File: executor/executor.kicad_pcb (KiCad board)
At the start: 4 copper layers, 58 x 58 mm, 130 parts, among them J1 XT30PW(2+2), J2 gh1.25, 3p, J3 Conn_01x04, Q1 WNM6006, Q2 WNM6006, Q3 WNM6006, Q4 WNM6006, Q5 WNM6006, Q6 WNM6006, U1 TPS5430DDAR, U2 DRV8323SRTAT, U3 GD32F303RETx, U4 TCAN4550RGYRQ1, U5 AS5047P-ATSM, U6 QMA7981, Y1 8M, Y2 40M

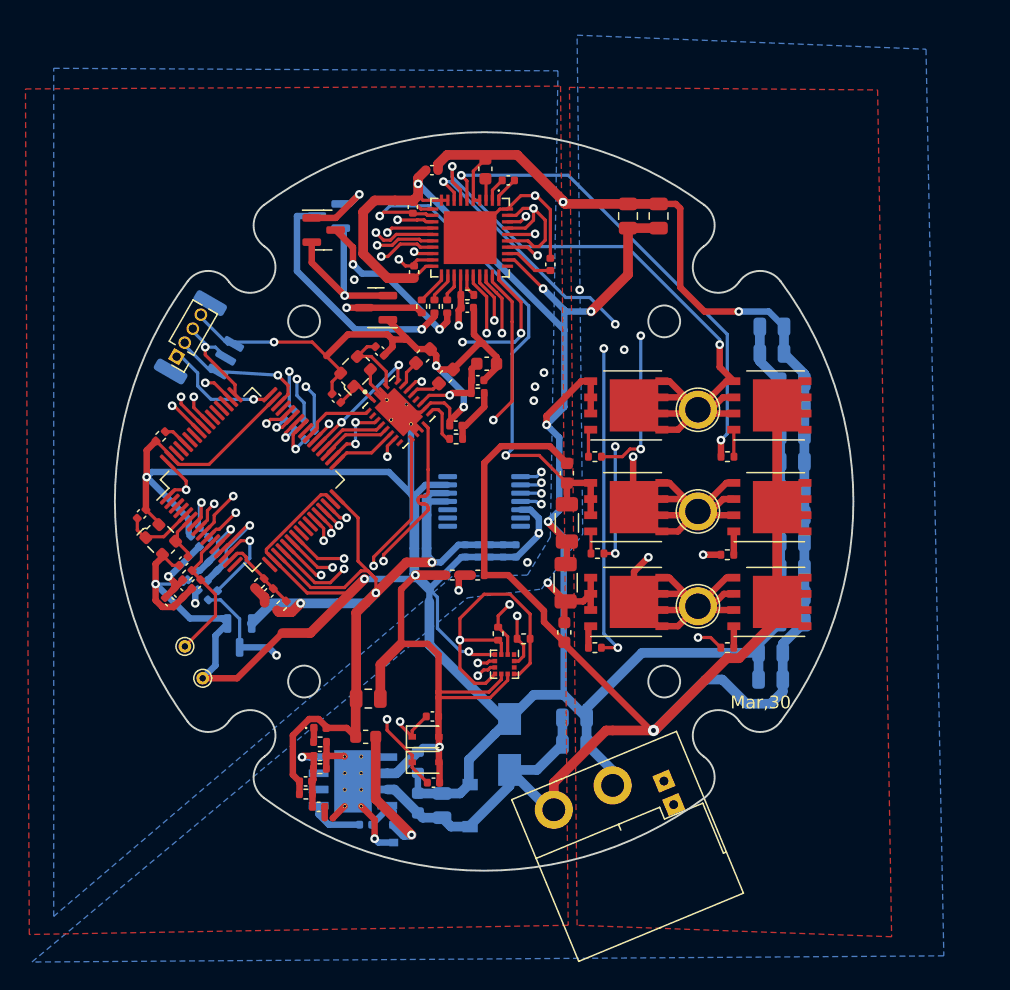
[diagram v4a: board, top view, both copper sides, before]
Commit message: [New] Complete PCB layout of executor v2.0
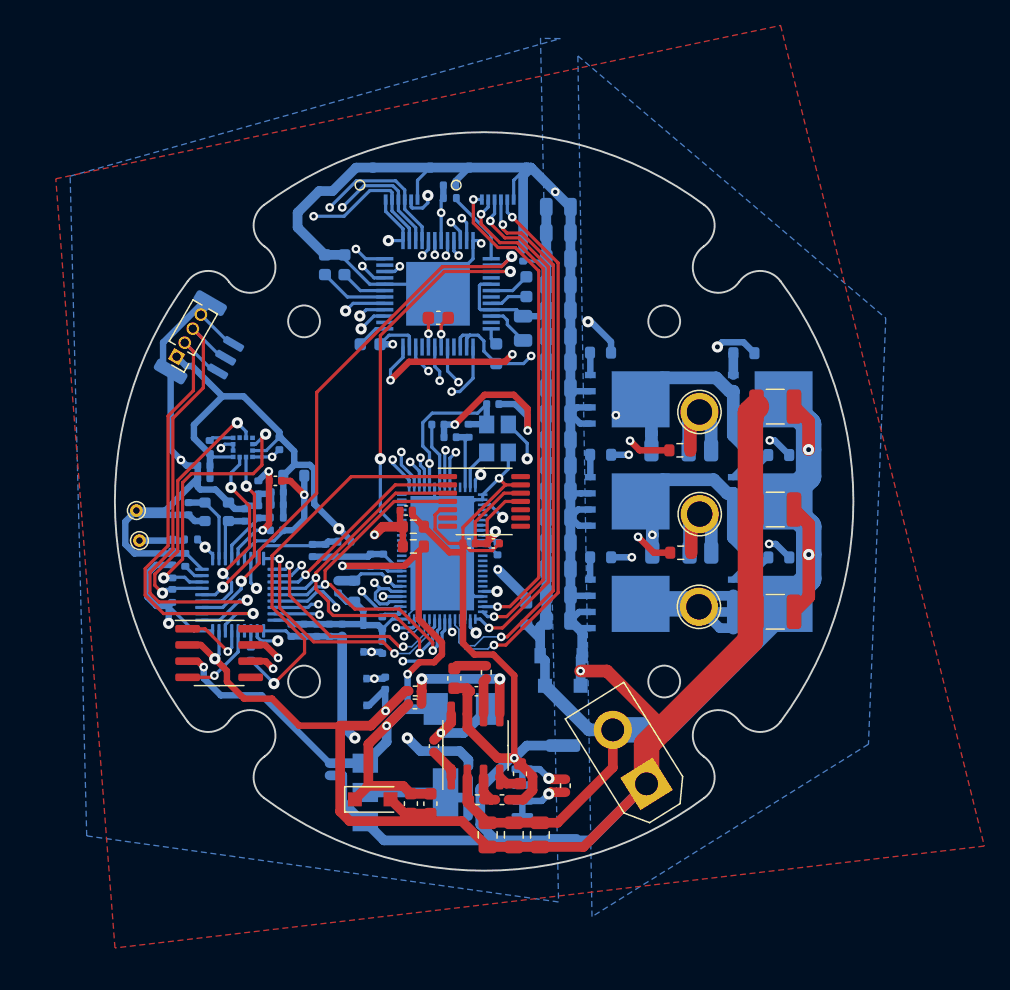
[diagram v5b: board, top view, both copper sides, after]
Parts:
- removed D10: ESD5Z3V3, Diode_SMD:D_SOD-523
- removed D6: BAV99, Package_TO_SOT_SMD:SOT-23
- removed D7: Blue, LED_SMD:LED_0402_1005Metric
- removed D8, D9: 12V, Diode_SMD:D_SOD-323
- removed FB1: 220R, Resistor_SMD:R_0603_1608Metric
- removed L1: 15uh, Inductor_SMD:L_0603_1608Metric
- removed NT1: NetTie, NetTie:NetTie-2_SMD_Pad0.5mm
- removed R34: 3k, Resistor_SMD:R_0402_1005Metric
- removed R37: 2.2k, 5%, Resistor_SMD:R_0402_1005Metric
- removed TP10: C, TestPoint:TestPoint_Plated_Hole_D2.0mm
- removed TP13: NTC+, TestPoint:TestPoint_THTPad_D1.0mm_Drill0.5mm
- removed TP14: NTC-, TestPoint:TestPoint_THTPad_D1.0mm_Drill0.5mm
- removed TP7: A, TestPoint:TestPoint_Plated_Hole_D2.0mm
- removed TP8: B, TestPoint:TestPoint_Plated_Hole_D2.0mm
- removed Y2: 40M, Oscillator:Oscillator_SMD_ECS_2520MV-xxx-xx-4Pin_2.5x2.0mm
- added C24: 10uF/50V/0805, Capacitor_SMD:C_0805_2012Metric, B.Cu at (80.8, 57.2)
- added C26: 100nF/100V/0805, Capacitor_SMD:C_0805_2012Metric, B.Cu at (80.8, 36.9)
- added C28: 470nF/50V/0603, Capacitor_SMD:C_0603_1608Metric, B.Cu at (66.0, 47.7)
- added C30: 470nF/50V/0603, Capacitor_SMD:C_0603_1608Metric, B.Cu at (76.0, 48.4)
- added C67: 22uF/6.3V/0402, Capacitor_SMD:C_0402_1005Metric, B.Cu at (74.2, 82.8)
- added C68: 47uf/50V/0603, Capacitor_SMD:C_0603_1608Metric, F.Cu at (69.2, 83.7)
- added C69: 47uf/50V/0603, Capacitor_SMD:C_0603_1608Metric, F.Cu at (70.8, 83.7)
- added C70: 100nF/10V/0402, Capacitor_SMD:C_0402_1005Metric, B.Cu at (50.5, 63.4)
- added C71: 100pF/50V/0402, Capacitor_SMD:C_0402_1005Metric, B.Cu at (67.2, 74.3)
- added C72: 100pF/50V/0402, Capacitor_SMD:C_0402_1005Metric, B.Cu at (67.0, 71.5)
- added C73: 2.2uF/50V/0603, Capacitor_SMD:C_0603_1608Metric, B.Cu at (62.5, 41.4)
- added J4: CAN_FD, Connector_JST:JST_GH_SM04B-GHS-TB_1x04-1MP_P1.25mm_Horizontal, B.Cu at (79.8, 82.9)
- added J5: RTMI, Rolling_Custom:FH34SRJ-6S-0.5SH50, B.Cu at (76.1, 35.2)
- added J6: DebugSPI, Rolling_Custom:FH34SRJ-6S-0.5SH50, B.Cu at (68.5, 35.2)
- added L3: 15uh/SLO0530H150MTT, Inductor_SMD:L_Sunlord_MWSA0518_5.4x5.2mm, B.Cu at (73.2, 76.3)
- added L4: LQW15AN1N3D10D, Inductor_SMD:L_0402_1005Metric, B.Cu at (73.8, 81.3)
- added R11: 22R/1%/0603, Resistor_SMD:R_0603_1608Metric, B.Cu at (84.2, 56.3)
- added R24: 20.5k/0402, Resistor_SMD:R_0402_1005Metric, F.Cu at (76.4, 83.4)
- added R25: 10k/5%/0402, Resistor_SMD:R_0402_1005Metric, B.Cu at (51.5, 64.6)
- added R26: 10k/5%/0402, Resistor_SMD:R_0402_1005Metric, B.Cu at (64.0, 63.2)
- added TP1: U, TestPoint:TestPoint_Plated_Hole_D2.0mm, F.Cu at (91.9, 53.0)
- added TP2: V, TestPoint:TestPoint_Plated_Hole_D2.0mm, F.Cu at (91.9, 61.0)
- added TP3: W, TestPoint:TestPoint_Plated_Hole_D2.0mm, F.Cu at (91.9, 68.3)
- added TP4: NTC+, TestPoint:TestPoint_THTPad_D1.0mm_Drill0.5mm, F.Cu at (47.9, 63.1)
- added TP5: NTC-, TestPoint:TestPoint_THTPad_D1.0mm_Drill0.5mm, F.Cu at (47.7, 60.7)
- added U7: AMS1117-3.3, Package_TO_SOT_SMD:SOT-223-3_TabPin2, B.Cu at (68.8, 82.9)
- added U8: GD32C103TBUx, Rolling_Custom:QFN-36-1EP_6x6mm_P0.5mm, B.Cu at (55.7, 67.3)
- added X1: X1G004241012811, Crystal:Crystal_SMD_3225-4Pin_3.2x2.5mm, B.Cu at (76.0, 55.1)
- C1, C11, C13, C3, C4, C7, C8: value 10uF, 20%, 50V -> 100nF/50V/0402; footprint Capacitor_SMD:C_0805_2012Metric -> Capacitor_SMD:C_0402_1005Metric
- C10: value 10nf 50V -> 2.2uF/100V/1210; footprint Capacitor_SMD:C_0402_1005Metric -> Capacitor_SMD:C_1210_3225Metric; moved to F.Cu
- C12: value 100uf 50V -> 2.2uF/50V/0603; footprint Capacitor_SMD:C_0805_2012Metric -> Capacitor_SMD:C_0603_1608Metric; moved to B.Cu
- C14: value 10uF, 20%, 50V -> 22nF/50V/0603; footprint Capacitor_SMD:C_0805_2012Metric -> Capacitor_SMD:C_0603_1608Metric
- C15, C18, C20: value 10uF, 20%, 50V -> 10uF/50V/0805
- C16: value 1.5nf 50V -> 10uF/50V/0805; footprint Capacitor_SMD:C_0402_1005Metric -> Capacitor_SMD:C_0805_2012Metric; moved to B.Cu
- C17: value 1uF, 10%, 50V -> 100nF/10V/0402; footprint Capacitor_SMD:C_0603_1608Metric -> Capacitor_SMD:C_0402_1005Metric; moved to F.Cu
- C19: value 10uF, 20%, 50V -> 100nF/100V/0805
- C2: value 10uF, 20%, 50V -> 4.7uF/50V/0402; footprint Capacitor_SMD:C_0805_2012Metric -> Capacitor_SMD:C_0402_1005Metric
- C21: value 10uF, 20%, 50V -> 1uF/10V/0402; footprint Capacitor_SMD:C_0805_2012Metric -> Capacitor_SMD:C_0402_1005Metric; moved to F.Cu
- C22: value 100nf 50V -> 10uF/50V/0805; footprint Capacitor_SMD:C_0402_1005Metric -> Capacitor_SMD:C_0805_2012Metric; moved to B.Cu
- C23: value 150pf 50V -> 10uF/50V/0805; footprint Capacitor_SMD:C_0402_1005Metric -> Capacitor_SMD:C_0805_2012Metric; moved to B.Cu
- C25, C37: value 1uF, 10%, 50V -> 10uF/50V/0805; footprint Capacitor_SMD:C_0603_1608Metric -> Capacitor_SMD:C_0805_2012Metric; moved to B.Cu
- C27, C33: value 100nF, 10%, 10V -> 10uF/50V/0805; footprint Capacitor_SMD:C_0402_1005Metric -> Capacitor_SMD:C_0805_2012Metric; moved to B.Cu
- C29: value 1uF, 10%, 50V -> 470nF/50V/0603
- C31, C34: value 4.7uF, 20%, 50V -> 10uF/50V/0805; moved to B.Cu
- C32: value 1nF, 10%, 50V -> 10nF/10V/0402; moved to B.Cu
- C35: value 1nF, 10%, 50V -> 2.2uF/10V0402; moved to B.Cu
- C36: value 100nF, 10%, 50V -> 10uF/50V/0805; footprint Capacitor_SMD:C_0402_1005Metric -> Capacitor_SMD:C_0805_2012Metric; moved to B.Cu
- C38: value 20pF, 10%, 10V -> 100nF/10V/0402; moved to B.Cu
- C39: value 100nF, 10%, 10V -> 10uF/50V/0805; footprint Capacitor_SMD:C_0402_1005Metric -> Capacitor_SMD:C_0805_2012Metric
- C40: value 10uF, 10%, 10V -> 10uF/50V/0805; footprint Capacitor_SMD:C_0402_1005Metric -> Capacitor_SMD:C_0805_2012Metric; moved to B.Cu
- C41: value 100nF, 10%, 10V -> 10pf/50V/0402; moved to F.Cu
- C42: value 20pF, 10%, 10V -> 10uF/10V/0402; moved to B.Cu
- C43: value 100nF, 10%, 10V -> 100nF/50V/0402; moved to B.Cu
- C44, C46: value 100nF, 10%, 10V -> 100nF/10V/0402
- C45: value 10uF, 10%, 10V -> 1.5nf/50V/0603; footprint Capacitor_SMD:C_0402_1005Metric -> Capacitor_SMD:C_0603_1608Metric; moved to F.Cu
- C47: value 4.7uF, 10%, 10V -> 10uF/10V/0402
- C48: value 1uF, 10%, 10V -> 100nF/10V/0402
- C49: value 47nF, 10%, 50V -> 100nF/10V/0402; moved to B.Cu
- C5, C9: value 10uF, 20%, 50V -> 2.2uF/100V/1210; footprint Capacitor_SMD:C_0805_2012Metric -> Capacitor_SMD:C_1210_3225Metric; moved to F.Cu
- C50: value 1uF, 10%, 10V -> 20pF/10V/0402
- C51: value 100nF, 10%, 10V -> 4.7uF/50V/0805; footprint Capacitor_SMD:C_0402_1005Metric -> Capacitor_SMD:C_0805_2012Metric; moved to F.Cu
- C52: value 100nF, 10%, 10V -> 100nF/10V/0402; moved to B.Cu
- C53: value 10pF, 10%, 50V -> 100nF/50V/0402
- C54: value 10nF, 10%, 50V -> 4.7uF/50V/0805; footprint Capacitor_SMD:C_0402_1005Metric -> Capacitor_SMD:C_0805_2012Metric
- C55: value 10pF, 10%, 50V -> 10uf/50V/0805; footprint Capacitor_SMD:C_0402_1005Metric -> Capacitor_SMD:C_0805_2012Metric
- C56: value 10nF, 10%, 10V -> 4.7uF/10V/0402
- C57: value 2.2uF, 10%, 10V -> 20pF/10V/0402
- C58: value 100nnF, 10%, 10V -> 1uF/10V/0402
- C59: value 470nF, 10%, 50V -> 100nF/10V/0402; footprint Capacitor_SMD:C_0603_1608Metric -> Capacitor_SMD:C_0402_1005Metric; moved to B.Cu
- C6: value 4.7uF 50V -> 100nF/50V/0402; footprint Capacitor_SMD:C_0805_2012Metric -> Capacitor_SMD:C_0402_1005Metric
- C60: value 100pF, 10%, 10V -> 100nF/10V/0402; moved to B.Cu
- C61: value 100nF, 10%, 10V -> 8.2nf/50V/0603; footprint Capacitor_SMD:C_0402_1005Metric -> Capacitor_SMD:C_0603_1608Metric; moved to F.Cu
- C62: value 100pF, 10%, 10V -> 10uf/50V/0402; moved to B.Cu
- C63: value 1uF, 10%, 10V -> 100nF/50V/0402
- C64: value 100nF, 10%, 50V -> 100nF/10V/0402
- C65: value 10uF, 10%, 50V -> 10uf/50V/0402; footprint Capacitor_SMD:C_0603_1608Metric -> Capacitor_SMD:C_0402_1005Metric; moved to B.Cu
- C66: value 10uF, 10%, 50V -> 100nF/50V/0402; footprint Capacitor_SMD:C_0603_1608Metric -> Capacitor_SMD:C_0402_1005Metric; moved to B.Cu
- D2: value BAV99 -> BZT52C24; footprint Package_TO_SOT_SMD:SOT-23 -> Diode_SMD:D_SOD-123F
- D3: value 30V -> BZT52C5V1S; footprint Diode_SMD:D_SMA -> Diode_SMD:D_SOD-123F; moved to F.Cu
- D4: value BAV99 -> 12V; footprint Package_TO_SOT_SMD:SOT-23 -> Diode_SMD:D_SOD-323; moved to B.Cu
- D5: value BAV99 -> 12V; footprint Package_TO_SOT_SMD:SOT-23 -> Diode_SMD:D_SOD-323
- J1: value XT30PW(2+2) -> PowerOutput; footprint Rolling_Custom:XT30PW(2+2) -> Connector_AMASS:AMASS_XT30UPB-M_1x02_P5.0mm_Vertical
- J2: value gh1.25, 3p -> SWD_DBG_Mounting
- J3: value Conn_01x04 -> SWD_DBG
- L2: value 20R -> FCM1608KF-100T07; footprint Resistor_SMD:R_0402_1005Metric -> Resistor_SMD:R_0603_1608Metric
- Q1, Q2, Q3, Q4, Q5, Q6: value WNM6006 -> BSC0702LS; footprint Rolling_Custom:PDFN5X6-8L -> Package_TO_SOT_SMD:TDSON-8-1; moved to B.Cu
- R1, R7: value 0 -> 22R/1%/0603; footprint Resistor_SMD:R_0402_1005Metric -> Resistor_SMD:R_0603_1608Metric
- R10: value 549R -> 22R/1%/0603; footprint Resistor_SMD:R_0201_0603Metric -> Resistor_SMD:R_0603_1608Metric; moved to B.Cu
- R12, R13: value 0 -> 22R/1%/0603; footprint Resistor_SMD:R_0402_1005Metric -> Resistor_SMD:R_0603_1608Metric; moved to B.Cu
- R14, R15: value 10k, 5% -> 4.7k/5%/0402; moved to B.Cu
- R16: value 0.001R -> 4k7/1%/0603; footprint Resistor_SMD:R_1206_3216Metric -> Resistor_SMD:R_0603_1608Metric; moved to B.Cu
- R17: value 10k, 5% -> 1k/1%/0603; footprint Resistor_SMD:R_0402_1005Metric -> Resistor_SMD:R_0603_1608Metric; moved to B.Cu
- R18: value 10k, 5% -> 64.9k/0402; moved to F.Cu
- R19: value 0 -> 0r/0402
- R2, R8: value 0 -> 0.003R/1%/1W/1206; footprint Resistor_SMD:R_0402_1005Metric -> Resistor_SMD:R_1206_3216Metric; moved to B.Cu
- R20: value 10k, 5% -> 10k/5%/0402; moved to B.Cu
- R21, R22: value 100R, 5% -> 4k7/1%/0603; footprint Resistor_SMD:R_0402_1005Metric -> Resistor_SMD:R_0603_1608Metric
- R23: value 100R, 5% -> 169k/0402
- R27: value 10k, 5% -> 10k/5%/3477K/0402; moved to B.Cu
- R28: value 0R, 5% -> 10.2k/0402; moved to F.Cu
- R29: value 0R, 5% -> 1.96k/0402; moved to F.Cu
- R3: value 10k -> 0.003R/1%/1W/1206; footprint Resistor_SMD:R_0402_1005Metric -> Resistor_SMD:R_1206_3216Metric; moved to B.Cu
- R30: value 0R, 5% -> 10k/5%/0402
- R31: value 100R, 5% -> 120R/0402; moved to F.Cu
- R32: value 33k -> 4.7k/5%/0402; moved to B.Cu
- R33: value 330R, 5% -> 0R/0402; moved to B.Cu
- R36: value 2.2k, 5% -> 0R/0402; moved to B.Cu
- R4: value 5.9k -> 22R/1%/0603; footprint Resistor_SMD:R_0402_1005Metric -> Resistor_SMD:R_0603_1608Metric; moved to B.Cu
- R5: value 150k, 5% -> 22R/1%/0603; footprint Resistor_SMD:R_0402_1005Metric -> Resistor_SMD:R_0603_1608Metric; moved to B.Cu
- R6: value 10k, 5% -> 10k/1%/0402; moved to B.Cu
- R9: value 0.001R -> 0.003R/1%/1W/1206; moved to B.Cu
- U1: value TPS5430DDAR -> TMC4671-LA; footprint Rolling_Custom:TPS5430DDAR -> Rolling_Custom:QFN76_10P5X6P5_TRI
- U2: value DRV8323SRTAT -> TJA1042T; footprint Rolling_Custom:WQFN40 -> Package_SO:SOIC-8_3.9x4.9mm_P1.27mm
- U3: value GD32F303RETx -> TMC6200-TA; footprint Package_QFP:LQFP-64_10x10mm_P0.5mm -> Rolling_Custom:eTQFP48_9x9_TRI; moved to B.Cu
- U4: value TCAN4550RGYRQ1 -> QMA7981; footprint Rolling_Custom:VQFN20 -> Package_LGA:LGA-12_2x2mm_P0.5mm; moved to B.Cu
- U5: moved to F.Cu
- U6: value QMA7981 -> TPS54231; footprint Package_LGA:LGA-12_2x2mm_P0.5mm -> Package_SO:SOIC-8_3.9x4.9mm_P1.27mm
- Y1: moved to B.Cu
- moved R4 46.6 mm to (95.4, 48.4), turned to 180 degrees
- moved R10 45.4 mm to (98.1, 56.4), turned to 180 degrees
- moved C40 41.1 mm to (80.8, 38.9), turned to 0 degrees
- moved R3 39.3 mm to (89.6, 56.0)
- moved C49 39.2 mm to (59.9, 70.1), turned to 90 degrees
- moved R23 39.0 mm to (74.5, 83.4), turned to 0 degrees
- moved C55 38.9 mm to (75.3, 86.2), turned to -90 degrees
- moved U2 38.1 mm to (54.2, 71.9), turned to 0 degrees
- moved D4 36.4 mm to (65.7, 75.0), turned to -90 degrees
- moved C10 36.2 mm to (97.9, 68.7)
- moved C39 35.7 mm to (80.8, 40.9), turned to 0 degrees
- moved C65 35.5 mm to (74.2, 84.7)
- moved R36 34.4 mm to (72.3, 36.2), turned to 180 degrees
- moved C12 34.1 mm to (64.0, 41.4), turned to -90 degrees
- moved C66 33.6 mm to (74.2, 83.7), turned to 0 degrees
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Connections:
- C1 pad 1: +24V -> GND
- C1 pad 2: GNDA -> +3V3
- C10 pad 1: Net-(C10-Pad1) -> GND
- C10 pad 2: Net-(C10-Pad2) -> +24V
- C11 pad 1: +24V -> GND
- C11 pad 2: GNDA -> +24V
- C12 pad 2: +3V3 -> Net-(C12-Pad2)
- C13 pad 1: +24V -> GND
- C13 pad 2: GNDA -> +3V3
- C14 pad 1: +24V -> Net-(C14-Pad1)
- C14 pad 2: GNDA -> Net-(C14-Pad2)
- C15 pad 2: GNDA -> GND
- C16 pad 1: TPS_VSEN -> +24V
- C16 pad 2: +3V3 -> GND
- C17 pad 1: GNDA -> +3V3
- C17 pad 2: +24V -> GND
- C18 pad 2: GNDA -> GND
- C19 pad 2: GNDA -> Net-(C19-Pad2)
- C2 pad 1: +24V -> +5V
- C2 pad 2: GNDA -> GND
- C20 pad 2: GNDA -> GND
- C21 pad 1: +24V -> +3V3
- C21 pad 2: GNDA -> GND
- C22 pad 1: TPS_VSEN -> +24V
- C22 pad 2: Net-(C22-Pad2) -> GND
- C23 pad 1: TPS_VSEN -> +24V
- C25 pad 1: IBP -> +24V
- C25 pad 2: +24V -> GND
- C27 pad 1: GND -> +24V
- C27 pad 2: TEMP_BOARD -> GND
- C29 pad 1: ICP -> Net-(C29-Pad1)
- C29 pad 2: +24V -> BMV
- C3 pad 1: +24V -> GND
- C3 pad 2: GNDA -> +5V
- C31 pad 2: GNDA -> GND
- C32 pad 1: IBP -> +3V3
- C32 pad 2: GNDA -> GND
- C33 pad 1: GND -> +24V
- C33 pad 2: TEMP_MOTOR -> GND
- C34 pad 2: GNDA -> GND
- C35 pad 1: ICP -> +3V3
- C35 pad 2: GNDA -> GND
- C36 pad 2: GNDA -> GND
- C37 pad 2: VCP -> GND
- C38 pad 1: GND -> +3V3
- C38 pad 2: MCU_OSC_IN -> GND
- C39 pad 1: NRST -> +24V
- C4 pad 1: +24V -> GND
- C4 pad 2: GNDA -> Net-(C4-Pad2)
- C40 pad 1: GND -> +24V
- C40 pad 2: +3V3 -> GND
- C41 pad 1: +3V3 -> 5V_CMP
- C42 pad 2: MCU_OSC_OUT -> +3V3
- C43 pad 2: +3V3 -> ADC_VM
- C44 pad 1: +3V3 -> GND
- C44 pad 2: GND -> +3V3
- C45 pad 1: VREF_S -> Net-(C45-Pad1)
- C45 pad 2: VREF_D -> GND
- C46 pad 1: VREF_S -> NRST
- C46 pad 2: VREF_D -> GND
- C47 pad 1: +3V3 -> VREF-
- C47 pad 2: GND -> VREF+
- C48 pad 1: Net-(C48-Pad1) -> VREF-
- C48 pad 2: GND -> VREF+
- C49 pad 1: Net-(C49-Pad1) -> +3V3
- C49 pad 2: Net-(C49-Pad2) -> GND
- C5 pad 1: +24V -> GND
- C5 pad 2: GNDA -> +24V
- C50 pad 1: +3V3 -> GND
- C50 pad 2: GND -> MCU_OSC_IN
- C51 pad 1: +3V3 -> +24V
- C53 pad 2: TCAN_OSC_IN -> +2.5V_REF
- C54 pad 1: GND -> +24V
- C54 pad 2: Net-(C54-Pad2) -> GND
- C55 pad 1: GND -> +24V
- C55 pad 2: TCAN_OSC_OUT -> GND
- C57 pad 1: +3V3 -> GND
- C57 pad 2: GND -> MCU_OSC_OUT
- C59 pad 1: Net-(C59-Pad1) -> GND
- C59 pad 2: GND -> TEMP_BOARD
- C6 pad 1: +24V -> GND
- C6 pad 2: GNDA -> Net-(C6-Pad2)
- C60 pad 1: GND -> +3V3
- C60 pad 2: CAN_L -> GND
- C61 pad 1: +3V3 -> Net-(C61-Pad1)
- C62 pad 1: GND -> +5V
- C62 pad 2: CAN_H -> GND
- C63 pad 1: +3V3 -> +5V
- C64 pad 1: +24V -> Net-(C64-Pad1)
- C64 pad 2: GND -> Net-(C64-Pad2)
- C65 pad 1: +24V -> Net-(C65-Pad1)
- C66 pad 1: VCCOUT -> Net-(C65-Pad1)
- C7 pad 1: +24V -> GND
- C7 pad 2: GNDA -> Net-(C7-Pad2)
- C8 pad 1: +24V -> GND
- C8 pad 2: GNDA -> Net-(C8-Pad2)
- C9 pad 1: +24V -> GND
- C9 pad 2: GNDA -> +24V
- D1 pad 1: GNDA -> GND
- D2 pad 1: GND -> +24V
- D2 pad 2: +3V3 -> GND
- D3 pad 1: GNDA -> +5V
- D3 pad 2: +24V -> GND
- D4 pad 1: GND -> CANFD_L
- D4 pad 2: +3V3 -> GND
- D5 pad 1: GND -> CANFD_H
- D5 pad 2: +3V3 -> GND
- J1 pad 1: +24V -> GND
- J1 pad 2: GNDA -> +24V
- J2 pad MP: (no net) -> GND
- L2 pad 2: VREF_D -> VREF+
- Q1 pad 1: A -> BMU
- Q1 pad 2: A -> BMU
- Q1 pad 3: A -> BMU
- Q2 pad 1: GNDA -> GND
- Q2 pad 2: GNDA -> GND
- Q2 pad 3: GNDA -> GND
- Q2 pad 5: A -> BMU
- Q3 pad 1: B -> BMV
- Q3 pad 2: B -> BMV
- Q3 pad 3: B -> BMV
- Q4 pad 1: IBP -> GND
- Q4 pad 2: IBP -> GND
- Q4 pad 3: IBP -> GND
- Q4 pad 5: B -> BMV
- Q5 pad 1: C -> W
- Q5 pad 2: C -> W
- Q5 pad 3: C -> W
- Q6 pad 1: ICP -> GND
- Q6 pad 2: ICP -> GND
- Q6 pad 3: ICP -> GND
- Q6 pad 5: C -> W
- R1 pad 1: VGL_A -> USENSE
- R1 pad 2: Net-(Q2-Pad4) -> U
- R10 pad 1: Net-(C22-Pad2) -> HSV
- R10 pad 2: GND -> Net-(Q3-Pad4)
- R12 pad 1: VGH_C -> HSW
- R13 pad 1: VGL_C -> LSW
- R14 pad 1: +3V3 -> ACC_SDA
- R14 pad 2: TEMP_BOARD -> +3V3
- R15 pad 1: TEMP_BOARD -> ACC_SCL
- R15 pad 2: GND -> +3V3
- R16 pad 1: ICP -> +24V
- R16 pad 2: GNDA -> ADC_VM
- R17 pad 1: +3V3 -> ADC_VM
- R17 pad 2: TEMP_MOTOR -> GND
- R18 pad 1: +3V3 -> 5V_CMP
- R18 pad 2: NRST -> Net-(C45-Pad1)
- R19 pad 2: VREF_S -> VREF-
- R2 pad 1: VGH_A -> U
- R2 pad 2: Net-(Q1-Pad4) -> BMU
- R20 pad 1: Net-(R20-Pad1) -> +3V3
- R20 pad 2: +3V3 -> NRST
- R21 pad 1: ISENSE_A -> +5V
- R21 pad 2: Net-(R21-Pad2) -> +2.5V_REF
- R22 pad 1: ISENSE_B -> +2.5V_REF
- R22 pad 2: Net-(R22-Pad2) -> GND
- R23 pad 1: ISENSE_C -> +24V
- R27 pad 1: Net-(R27-Pad1) -> TEMP_BOARD
- R28 pad 1: Net-(R28-Pad1) -> +5V
- R28 pad 2: PWM_A -> 5V_FB
- R29 pad 1: Net-(R29-Pad1) -> 5V_FB
- R29 pad 2: PWM_B -> GND
- R3 pad 1: TPS_VSEN -> U
- R3 pad 2: +3V3 -> BMU
- R30 pad 1: Net-(R30-Pad1) -> +3V3
- R30 pad 2: PWM_C -> TEMP_MOTOR
- R31 pad 1: Net-(R31-Pad1) -> CANFD_H
- R31 pad 2: VSEN_BUS -> CANFD_L
- R32 pad 1: TCAN_WAKE -> Net-(R32-Pad1)
- R32 pad 2: Net-(C54-Pad2) -> +3V3
- R33 pad 1: Net-(D7-Pad1) -> ECD_SCS
- R33 pad 2: GND -> Net-(U8-Pad21)
- R36 pad 1: ACC_SDA -> Net-(R36-Pad1)
- R4 pad 1: TPS_VSEN -> HSU
- R4 pad 2: GND -> Net-(Q1-Pad4)
- R5 pad 1: +24V -> LSU
- R5 pad 2: VSEN_BUS -> Net-(Q2-Pad4)
- R6 pad 1: VSEN_BUS -> +3V3
- R6 pad 2: GND -> Net-(C4-Pad2)
- R7 pad 1: VGH_B -> VSENSE
- R7 pad 2: Net-(Q3-Pad4) -> V
- R8 pad 1: VGL_B -> V
- R8 pad 2: Net-(Q4-Pad4) -> BMV
- R9 pad 1: IBP -> V
- R9 pad 2: GNDA -> BMV
- U1 pad 1: Net-(C10-Pad1) -> DBG_SDI
- U1 pad 10: GND -> FOC_RXD
- U1 pad 11: GND -> FOC_TXD
- U1 pad 12: GND -> FOC_STATUS
- U1 pad 13: GND -> +3V3
- U1 pad 15: GND -> Net-(C6-Pad2)
- U1 pad 16: GND -> CURU
- U1 pad 17: GND -> +2.5V_REF
- U1 pad 2: unconnected-(U1-Pad2) -> +3V3
- U1 pad 3: unconnected-(U1-Pad3) -> GND
- U1 pad 4: TPS_VSEN -> DBG_SDO
- U1 pad 5: unconnected-(U1-Pad5) -> DBG_TRG
- U1 pad 6: GND -> FOC_SCS
- U1 pad 7: +24V -> EXE_SCK
- U1 pad 8: Net-(C10-Pad2) -> EXE_SDI
- U1 pad 9: GND -> EXE_SDO
- U2 pad 1: Net-(C49-Pad2) -> CANFD_TX
- U2 pad 2: Net-(C49-Pad1) -> GND
- U2 pad 3: VCP -> +5V
- U2 pad 4: +24V -> CANFD_RX
- U2 pad 5: +24V -> unconnected-(U2-Pad5)
- U2 pad 6: VGH_A -> CANFD_L
- U2 pad 7: A -> CANFD_H
- U2 pad 8: VGL_B -> unconnected-(U2-Pad8)
- U3 pad 1: +3V3 -> Net-(C28-Pad1)
- U3 pad 10: ISENSE_A -> CURV
- U3 pad 11: TEMP_MOTOR -> unconnected-(U3-Pad11)
- U3 pad 12: VREF_S -> +2.5V_REF
- U3 pad 13: VREF_D -> DRV_SCS
- U3 pad 14: Net-(R31-Pad1) -> EXE_SCK
- U3 pad 15: TEMP_BOARD -> EXE_SDI
- U3 pad 16: unconnected-(U3-Pad16) -> EXE_SDO
- U3 pad 17: unconnected-(U3-Pad17) -> UH
- U3 pad 18: GND -> UL
- U3 pad 20: DRV_SCS -> VH
- U3 pad 21: DRV_SCK -> VL
- U3 pad 22: DRV_SDO -> WH
- U3 pad 23: DRV_SDI -> WL
- U3 pad 24: unconnected-(U3-Pad24) -> GND
- U3 pad 25: unconnected-(U3-Pad25) -> Net-(R36-Pad1)
- U3 pad 26: unconnected-(U3-Pad26) -> DRV_FAULT
- U3 pad 27: ACC_INT2 -> DRV_EN
- U3 pad 28: ACC_INT1 -> unconnected-(U3-Pad28)
- U3 pad 29: ACC_SCL -> +24V
- U3 pad 3: unconnected-(U3-Pad3) -> LSW
- U3 pad 30: ACC_SDA -> Net-(C14-Pad2)
- U3 pad 31: GND -> unconnected-(U3-Pad31)
- U3 pad 32: +3V3 -> Net-(C14-Pad1)
- U3 pad 33: TCAN_SCS -> +24V
- U3 pad 34: TCAN_SCK -> Net-(C19-Pad2)
- U3 pad 35: TCAN_SDO -> unconnected-(U3-Pad35)
- U3 pad 36: TCAN_SDI -> Net-(C30-Pad1)
- U3 pad 37: TCAN_RST -> HSW
- U3 pad 38: TCAN_INT -> W
- U3 pad 39: TCAN_WKRQ -> W
- U3 pad 4: unconnected-(U3-Pad4) -> LSV
- U3 pad 41: Net-(R28-Pad1) -> VSENSE
- U3 pad 42: Net-(R29-Pad1) -> BMV
- U3 pad 43: Net-(R30-Pad1) -> HSV
- U3 pad 44: DRV_EN -> Net-(C29-Pad1)
- U3 pad 46: SWDIO -> USENSE
- U3 pad 47: GND -> BMU
- U3 pad 48: +3V3 -> HSU
- U3 pad 5: MCU_OSC_IN -> LSU
- U3 pad 6: MCU_OSC_OUT -> Net-(C73-Pad2)
- U3 pad 7: NRST -> Net-(C12-Pad2)
- U3 pad 8: ISENSE_C -> GND
- U3 pad 9: ISENSE_B -> CURU
- U4 pad 1: TCAN_OSC_IN -> unconnected-(U4-Pad1)
- U4 pad 10: CAN_L -> Net-(R32-Pad1)
- U4 pad 11: CAN_H -> unconnected-(U4-Pad11)
- U4 pad 12: TCAN_WAKE -> ACC_SCL
- U4 pad 2: TCAN_WKRQ -> ACC_SDA
- U4 pad 3: unconnected-(U4-Pad3) -> +3V3
- U4 pad 4: TCAN_SCK -> GND
- U4 pad 5: TCAN_SDI -> ACC_INT1
- U4 pad 6: TCAN_SDO -> ACC_INT2
- U4 pad 7: TCAN_SCS -> +3V3
- U4 pad 8: TCAN_INT -> GND
- U4 pad 9: unconnected-(U4-Pad9) -> GND
- U5 pad 2: ECD_SCK -> EXE_SCK
- U5 pad 3: ECD_MISO -> EXE_SDO
- U5 pad 4: ECD_MOSI -> EXE_SDI
- U6 pad 1: unconnected-(U6-Pad1) -> Net-(C64-Pad2)
- U6 pad 2: ACC_SDA -> +24V
- U6 pad 3: +3V3 -> Net-(R23-Pad2)
- U6 pad 4: GND -> Net-(C61-Pad1)
- U6 pad 5: ACC_INT1 -> 5V_FB
- U6 pad 6: ACC_INT2 -> 5V_CMP
- U6 pad 7: +3V3 -> GND
- U6 pad 8: GND -> Net-(C64-Pad1)
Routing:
- net GND: track 312.3 -> 500.2 mm, vias 14 -> 12
- net GNDA: track 183.0 -> 0.00 mm, vias 5 -> 0
- net +24V: track 218.8 -> 125.3 mm, vias 4 -> 2
- net EXE_SCK: track 0.00 -> 78.0 mm, vias 0 -> 3
- net EXE_SDO: track 0.00 -> 76.6 mm, vias 0 -> 3
- net EXE_SDI: track 0.00 -> 74.5 mm, vias 0 -> 3
- net C: track 68.6 -> 0.00 mm, vias 3 -> 0
- net +5V: track 0.00 -> 66.6 mm, vias 0 -> 4
- net B: track 64.2 -> 0.00 mm, vias 3 -> 0
- net FOC_SCS: track 0.00 -> 61.1 mm, vias 0 -> 3
- net A: track 57.1 -> 0.00 mm, vias 2 -> 0
- net CAN_L: track 55.8 -> 0.00 mm, vias 2 -> 0
- net CAN_H: track 53.8 -> 0.00 mm, vias 2 -> 0
- net ICP: track 52.4 -> 0.00 mm, vias 3 -> 0
- net VGH_C: track 51.9 -> 0.00 mm, vias 2 -> 0
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- added copper zone on B.Cu, net +24V
- added copper zone on In1.Cu, net GND
- added copper zone on In2.Cu, net GND
- removed copper zone on In2.Cu, net +24V
- removed copper zone on In1.Cu, net +3V3
- removed copper zone on B.Cu, net GNDA
- removed copper zone on F.Cu, net GNDA
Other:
- board text added: "Rolling/2.0"
- board text removed: "Mar,30"

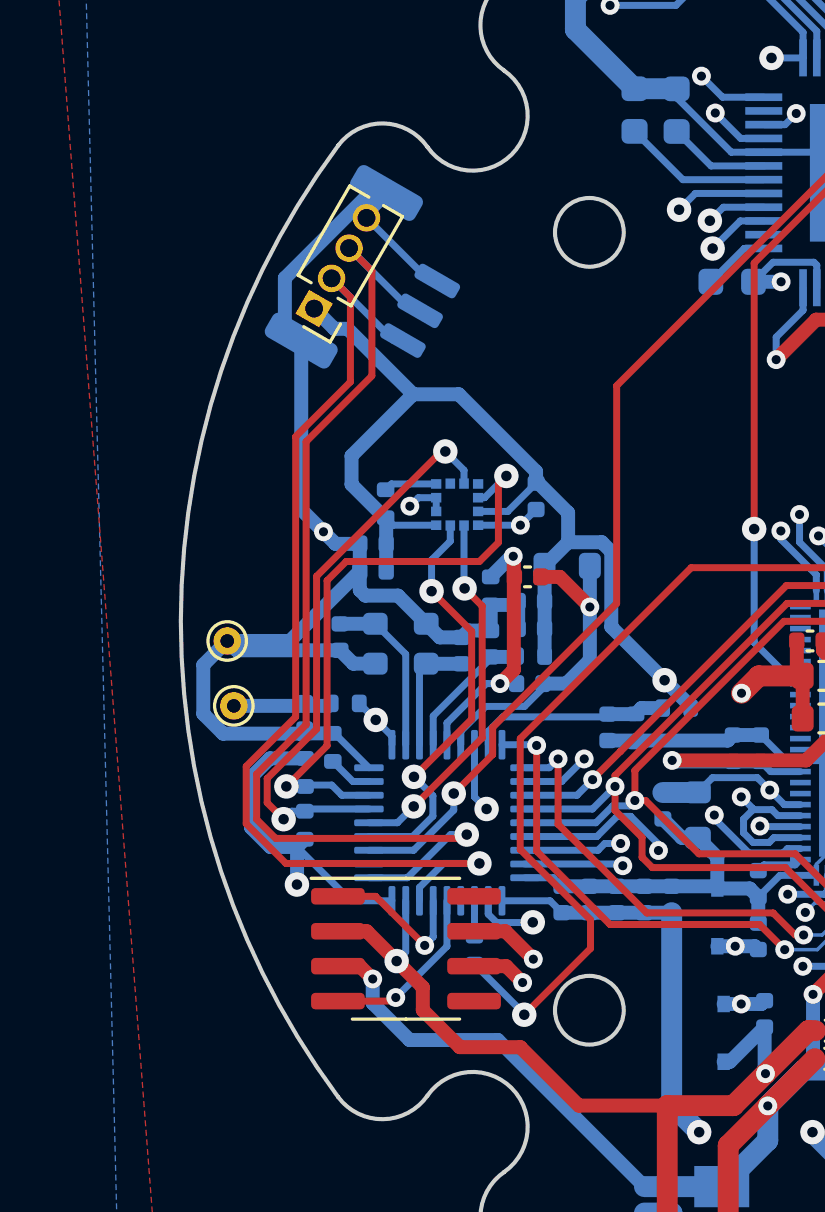
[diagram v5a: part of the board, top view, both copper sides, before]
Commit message: [Fix] Move components to avoid collisions
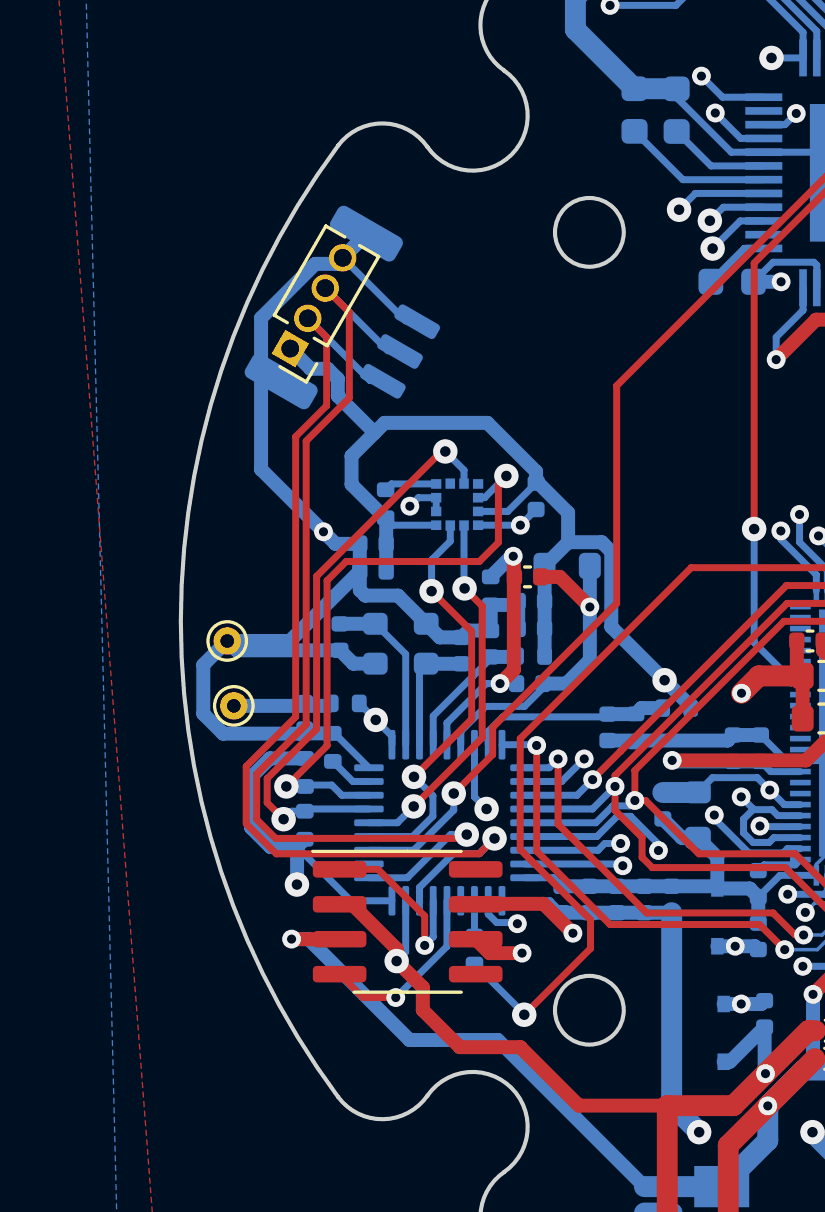
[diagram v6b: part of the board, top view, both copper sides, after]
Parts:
- moved J3 1.69 mm to (50.0, 50.1)
- moved J2 1.65 mm to (52.4, 49.3)
- moved U2 0.98 mm to (54.2, 70.9)
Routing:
- net +5V: track 66.6 -> 69.9 mm
- net SWCLK: track 38.6 -> 36.8 mm
- net +3V3: track 223.2 -> 222.2 mm
- net CANFD_TX: track 5.65 -> 6.62 mm
- net CANFD_L: track 35.3 -> 34.6 mm
- net CANFD_H: track 35.2 -> 34.6 mm
